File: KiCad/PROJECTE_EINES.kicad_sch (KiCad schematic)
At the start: 5 parts, among them J3 J_DEBUG

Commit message: Correció etapa d'alimentació e Inputs
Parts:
- renumbered J3 to J1, J_MOTOR_DOOR to J_MOTOR_DOOR1, R2 to R1
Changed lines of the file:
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@@
 		(dnp no)
 		(fields_autoplaced yes)
-		(property "Reference" "#PWR05"
+		(property "Reference" "#PWR01"
 			(at 26.67 107.95 0)
 			(effects
@@
 			(project ""
 				(path "/347831db-5db9-4aff-ad32-e56fd770e219"
-					(reference "#PWR05")
+					(reference "#PWR01")
 					(unit 1)
 				)
@@
 		(dnp no)
 		(fields_autoplaced yes)
-		(property "Reference" "#PWR06"
+		(property "Reference" "#PWR05"
 			(at 49.53 109.22 0)
 			(effects
@@
 			(project ""
 				(path "/347831db-5db9-4aff-ad32-e56fd770e219"
-					(reference "#PWR06")
+					(reference "#PWR05")
 					(unit 1)
 				)
@@
 		(dnp no)
 		(fields_autoplaced yes)
-		(property "Reference" "#PWR012"
+		(property "Reference" "#PWR02"
 			(at 30.48 54.61 0)
 			(effects
@@
 			(project "PROJECTE_EINES"
 				(path "/347831db-5db9-4aff-ad32-e56fd770e219"
-					(reference "#PWR012")
+					(reference "#PWR02")
 					(unit 1)
 				)
@@
 		(on_board yes)
 		(dnp no)
-		(property "Reference" "J3"
+		(property "Reference" "J1"
 			(at 22.225 16.51 0)
 			(effects
@@
 			(project "PROJECTE_EINES"
 				(path "/347831db-5db9-4aff-ad32-e56fd770e219"
-					(reference "J3")
+					(reference "J1")
 					(unit 1)
 				)
@@
 		(dnp no)
 		(fields_autoplaced yes)
-		(property "Reference" "#PWR014"
+		(property "Reference" "#PWR03"
 			(at 40.64 27.94 0)
 			(effects
@@
 			(project ""
 				(path "/347831db-5db9-4aff-ad32-e56fd770e219"
-					(reference "#PWR014")
+					(reference "#PWR03")
 					(unit 1)
 				)
@@
 		(dnp no)
 		(fields_autoplaced yes)
-		(property "Reference" "J_MOTOR_DOOR"
+		(property "Reference" "J_MOTOR_DOOR1"
 			(at 22.225 72.39 0)
 			(effects
@@
 			(project "PROJECTE_EINES"
 				(path "/347831db-5db9-4aff-ad32-e56fd770e219"
-					(reference "J_MOTOR_DOOR")
+					(reference "J_MOTOR_DOOR1")
 					(unit 1)
 				)
@@
 		(dnp no)
 		(fields_autoplaced yes)
-		(property "Reference" "R2"
+		(property "Reference" "R1"
 			(at 38.1 95.25 90)
 			(effects
@@
 			(project "PROJECTE_EINES"
 				(path "/347831db-5db9-4aff-ad32-e56fd770e219"
-					(reference "R2")
+					(reference "R1")
 					(unit 1)
 				)
@@
 		(dnp no)
 		(fields_autoplaced yes)
-		(property "Reference" "#PWR07"
+		(property "Reference" "#PWR04"
 			(at 40.64 34.29 0)
 			(effects
@@
 			(project "PROJECTE_EINES"
 				(path "/347831db-5db9-4aff-ad32-e56fd770e219"
-					(reference "#PWR07")
-					(unit 1)
-				)
+					(reference "#PWR04")
+					(unit 1)
+				)

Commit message: Actualizació Footprints
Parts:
- J_DEBUG1: renamed from J1; value J_DEBUG -> Conn_01x05_Pin; footprint (none) -> Connector_PinHeader_2.54mm:PinHeader_1x05_P2.54mm_Vertical
- J_MOTOR_DOOR1, J_MOTOR_WIN1, J_PWR1: footprint (none) -> TerminalBlock:TerminalBlock_MaiXu_MX126-5.0-02P_1x02_P5.00mm
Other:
- sheet ETAPA DE POTÈNCIA renamed ETAPA DE ALIMENTACIÓ
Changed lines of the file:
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@@
 			)
 		)
-		(property "Footprint" ""
+		(property "Footprint" "TerminalBlock:TerminalBlock_MaiXu_MX126-5.0-02P_1x02_P5.00mm"
 			(at 21.59 63.5 0)
 			(effects
@@
 		(on_board yes)
 		(dnp no)
-		(property "Reference" "J1"
+		(property "Reference" "J_DEBUG1"
 			(at 22.225 16.51 0)
 			(effects
@@
 			)
 		)
-		(property "Value" "J_DEBUG"
+		(property "Value" "Conn_01x05_Pin"
 			(at 22.225 19.05 0)
 			(effects
@@
 			)
 		)
-		(property "Footprint" ""
+		(property "Footprint" "Connector_PinHeader_2.54mm:PinHeader_1x05_P2.54mm_Vertical"
 			(at 21.59 26.67 0)
 			(effects
@@
 			(project "PROJECTE_EINES"
 				(path "/347831db-5db9-4aff-ad32-e56fd770e219"
-					(reference "J1")
+					(reference "J_DEBUG1")
 					(unit 1)
 				)
@@
 			)
 		)
-		(property "Footprint" ""
+		(property "Footprint" "TerminalBlock:TerminalBlock_MaiXu_MX126-5.0-02P_1x02_P5.00mm"
 			(at 22.86 44.45 0)
 			(effects
@@
 			)
 		)
-		(property "Footprint" ""
+		(property "Footprint" "TerminalBlock:TerminalBlock_MaiXu_MX126-5.0-02P_1x02_P5.00mm"
 			(at 21.59 77.47 0)
 			(effects
@@
 			(color 0 0 0 0.0000)
 		)
-		(property "Sheetname" "ETAPA DE POTÈNCIA"
+		(property "Sheetname" "ETAPA DE ALIMENTACIÓ"
 			(at 72.39 19.6084 0)
 			(effects

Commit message: Versió final Esquematic
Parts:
- R1: footprint (none) -> Resistor_SMD:R_0805_2012Metric
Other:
- sheet BUS CAN renamed COMUNICACIONS
- sheet SENSOR DE CORRENT renamed SENSORS
- removed sheet DRIVER DEL MOTOR FINESTRA
- removed sheet DRIVER MOTOR PORTA
- removed sheet ETAPA DE ALIMENTACIÓ
- removed sheet SENSOR RFID
- added sheet ETAPA DE ALIMENTACIO (ETAPA_ALIMENTACIO_sch.kicad_sch)
- added sheet ETAPA DE POTENCIA (ETAPA_POTENICA.kicad_sch)
- sheet COMUNICACIONS ports: added CAN_RX, CAN_TX; removed CANRX, CANTX
- sheet INPUTS ports: added DOOR_BTN_CLOSED, DOOR_BTN_OPEN, DOOR_LOCK_SW, DOOR_UNLOCK_SW; removed none
- sheet MICROCONTROLADOR I DEBUG ports: added CAN_RX, CAN_TX, DOOR_BTN_CLOSED, DOOR_BTN_OPEN, DOOR_DIAGA, DOOR_DIAGB, DOOR_INA, DOOR_INB, DOOR_LIMIT_CLOSE, DOOR_LIMIT_OPEN, DOOR_LOCK_SW, DOOR_PWM, DOOR_UNLOCK_SW; removed GND
- sheet SENSORS ports: added RFID_CS, RFID_MISO, RFID_MOSI, RFID_RST, RFID_SCK, WIN_CURRENT_ADC; removed NO
- note added: "POTENCIA"
- note added: "SENSORS"
- note removed: "MOTOR FINESTRA"
- note removed: "MOTOR PORTA"
- note removed: "SENSOR FINAL DE CARRERA"
- note removed: "SENSOR RFID"
- moved on the sheet: R1

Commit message: 1ra versióPCB
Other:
- sheet ETAPA DE POTENCIA ports: added DOOR_MOTOR_A, DOOR_MOTOR_B, WIN_MOTOR_A, WIN_MOTOR_B; removed DOOR_OUTA, DOOR_OUTB, WIN_OUTA, WIN_OUTB
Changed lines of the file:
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@@
 		)
 	)
-	(global_label "WIN_OUTA"
+	(global_label "WIN_MOTOR_B"
 		(shape output)
 		(at 248.92 107.95 0)
@@
 		)
 	)
-	(global_label "DOOR_OUTA"
+	(global_label "DOOR_MOTOR_A"
 		(shape output)
 		(at 201.93 104.14 180)
@@
 		)
 	)
-	(global_label "WIN_OUTB"
+	(global_label "WIN_MOTOR_A"
 		(shape output)
 		(at 248.92 104.14 0)
@@
 		)
 	)
-	(global_label "DOOR_OUTB"
+	(global_label "DOOR_MOTOR_B"
 		(shape output)
 		(at 201.93 107.95 180)
@@
 			)
 		)
-		(pin "DOOR_OUTA" output
+		(pin "DOOR_MOTOR_A" output
 			(at 201.93 104.14 180)
 			(effects
@@
 			)
 		)
-		(pin "DOOR_OUTB" output
+		(pin "DOOR_MOTOR_B" output
 			(at 201.93 107.95 180)
 			(effects
@@
 			)
 		)
-		(pin "WIN_OUTA" output
+		(pin "WIN_MOTOR_A" output
 			(at 248.92 107.95 0)
 			(effects
@@
 			)
 		)
-		(pin "WIN_OUTB" output
+		(pin "WIN_MOTOR_B" output
 			(at 248.92 104.14 0)
 			(effects

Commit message: Inputs
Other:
- sheet INPUTS ports: added DOOR_LOCK/UNLOCK; removed DOOR_BTN_CLOSED, DOOR_BTN_OPEN, DOOR_LOCK_SW, DOOR_UNLOCK_SW
- sheet MICROCONTROLADOR I DEBUG ports: added DOOR_LOCK/UNLOCK; removed DOOR_BTN_CLOSED, DOOR_BTN_OPEN, DOOR_LOCK_SW, DOOR_UNLOCK_SW
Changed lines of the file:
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@@
-		)
-	)
-	(global_label "DOOR_LOCK_SW"
-		(shape input)
-		(at 153.67 125.73 0)
-		(effects
-			(font
-				(size 1.27 1.27)
-			)
-			(justify left)
-		)
-		(property "Intersheetrefs" "${INTERSHEET_REFS}"
-			(at 153.67 125.73 0)
-			(effects
-				(font
-					(size 1.27 1.27)
-				)
-				(hide yes)
-			)
-		)
-	)
-	(global_label "DOOR_LOCK_SW"
-		(shape output)
-		(at 248.92 147.32 0)
-		(effects
-			(font
-				(size 1.27 1.27)
-			)
-			(justify left)
-		)
-		(property "Intersheetrefs" "${INTERSHEET_REFS}"
-			(at 248.92 147.32 0)
-			(effects
-				(font
-					(size 1.27 1.27)
-				)
-				(hide yes)
-			)
 		)
 	)
@@
 		(property "Intersheetrefs" "${INTERSHEET_REFS}"
 			(at 248.92 76.2 0)
-			(effects
-				(font
-					(size 1.27 1.27)
-				)
-				(hide yes)
-			)
-		)
-	)
-	(global_label "DOOR_BTN_OPEN"
-		(shape input)
-		(at 153.67 123.19 0)
-		(effects
-			(font
-				(size 1.27 1.27)
-			)
-			(justify left)
-		)
-		(property "Intersheetrefs" "${INTERSHEET_REFS}"
-			(at 153.67 123.19 0)
 			(effects
 				(font
@@
 		)
 	)
-	(global_label "DOOR_UNLOCK_SW"
-		(shape output)
-		(at 248.92 149.86 0)
-		(effects
-			(font
-				(size 1.27 1.27)
-			)
-			(justify left)
-		)
-		(property "Intersheetrefs" "${INTERSHEET_REFS}"
-			(at 248.92 149.86 0)
-			(effects
-				(font
-					(size 1.27 1.27)
-				)
-				(hide yes)
-			)
-		)
-	)
 	(global_label "UART_TX"
 		(shape output)
@@
 		(property "Intersheetrefs" "${INTERSHEET_REFS}"
 			(at 82.55 113.03 0)
-			(effects
-				(font
-					(size 1.27 1.27)
-				)
-				(hide yes)
-			)
-		)
-	)
-	(global_label "DOOR_UNLOCK_SW"
-		(shape input)
-		(at 153.67 128.27 0)
-		(effects
-			(font
-				(size 1.27 1.27)
-			)
-			(justify left)
-		)
-		(property "Intersheetrefs" "${INTERSHEET_REFS}"
-			(at 153.67 128.27 0)
 			(effects
 				(font
@@
 		)
 	)
-	(global_label "DOOR_BTN_CLOSED"
-		(shape input)
-		(at 153.67 120.65 0)
-		(effects
-			(font
-				(size 1.27 1.27)
-			)
-			(justify left)
-		)
-		(property "Intersheetrefs" "${INTERSHEET_REFS}"
-			(at 153.67 120.65 0)
-			(effects
-				(font
-					(size 1.27 1.27)
-				)
-				(hide yes)
-			)
-		)
-	)
 	(global_label "WIN_MOTOR_A"
 		(shape output)
@@
 		)
 	)
-	(global_label "DOOR_BTN_CLOSED"
-		(shape output)
-		(at 248.92 144.78 0)
-		(effects
-			(font
-				(size 1.27 1.27)
-			)
-			(justify left)
-		)
-		(property "Intersheetrefs" "${INTERSHEET_REFS}"
-			(at 248.92 144.78 0)
-			(effects
-				(font
-					(size 1.27 1.27)
-				)
-				(hide yes)
-			)
-		)
-	)
 	(global_label "DOOR_MOTOR_B"
 		(shape output)
@@
 		)
 	)
-	(global_label "DOOR_BTN_OPEN"
-		(shape output)
-		(at 248.92 142.24 0)
-		(effects
-			(font
-				(size 1.27 1.27)
-			)
-			(justify left)
-		)
-		(property "Intersheetrefs" "${INTERSHEET_REFS}"
-			(at 248.92 142.24 0)
-			(effects
-				(font
-					(size 1.27 1.27)
-				)
-				(hide yes)
-			)
-		)
-	)
 	(global_label "RFID_MISO"
 		(shape input)
@@
 		)
 	)
+	(global_label "DOOR_LOCK{slash}UNLOCK"
+		(shape input)
+		(at 153.67 120.65 0)
+		(fields_autoplaced yes)
+		(effects
+			(font
+				(size 1.27 1.27)
+			)
+			(justify left)
+		)
+		(property "Intersheetrefs" "${INTERSHEET_REFS}"
+			(at 176.6125 120.65 0)
+			(effects
+				(font
+					(size 1.27 1.27)
+				)
+				(justify left)
+				(hide yes)
+			)
+		)
+	)
 	(global_label "WIN_BTN_UP"
 		(shape output)
@@
 					(size 1.27 1.27)
 				)
+				(hide yes)
+			)
+		)
+	)
+	(global_label "DOOR_LOCK{slash}UNLOCK"
+		(shape output)
+		(at 248.92 146.05 0)
+		(fields_autoplaced yes)
+		(effects
+			(font
+				(size 1.27 1.27)
+			)
+			(justify left)
+		)
+		(property "Intersheetrefs" "${INTERSHEET_REFS}"
+			(at 271.8625 146.05 0)
+			(effects
+				(font
+					(size 1.27 1.27)
+				)
+				(justify left)
 				(hide yes)
 			)
@@
 			)
 		)
-		(pin "DOOR_BTN_CLOSED" input
-			(at 153.67 120.65 0)
-			(effects
-				(font
-					(size 1.27 1.27)
-				)
-				(justify right)
-			)
-		)
-		(pin "DOOR_BTN_OPEN" input
-			(at 153.67 123.19 0)
-			(effects
-				(font
-					(size 1.27 1.27)
-				)
-				(justify right)
-			)
-		)
 		(pin "DOOR_DIAGA" input
 			(at 153.67 138.43 0)
@@
 			)
 		)
-		(pin "DOOR_LOCK_SW" input
-			(at 153.67 125.73 0)
-			(effects
-				(font
-					(size 1.27 1.27)
-				)
-				(justify right)
-			)
-		)
 		(pin "DOOR_PWM" output
 			(at 153.67 140.97 0)
@@
 			)
 		)
-		(pin "DOOR_UNLOCK_SW" input
-			(at 153.67 128.27 0)
+		(pin "DOOR_LOCK{slash}UNLOCK" input
+			(at 153.67 120.65 0)
 			(effects
 				(font
@@
 			)
 		)
-		(pin "DOOR_BTN_CLOSED" output
-			(at 248.92 144.78 0)
-			(effects
-				(font
-					(size 1.27 1.27)
-				)
-				(justify right)
-			)
-		)
-		(pin "DOOR_BTN_OPEN" output
-			(at 248.92 142.24 0)
-			(effects
-				(font
-					(size 1.27 1.27)
-				)
-				(justify right)
-			)
-		)
-		(pin "DOOR_LOCK_SW" output
-			(at 248.92 147.32 0)
-			(effects
-				(font
-					(size 1.27 1.27)
-				)
-				(justify right)
-			)
-		)
-		(pin "DOOR_UNLOCK_SW" output
-			(at 248.92 149.86 0)
-			(effects
-				(font
+		(pin "DOOR_LOCK{slash}UNLOCK" output
+			(at 248.92 146.05 0)
+			(effects
+				(font

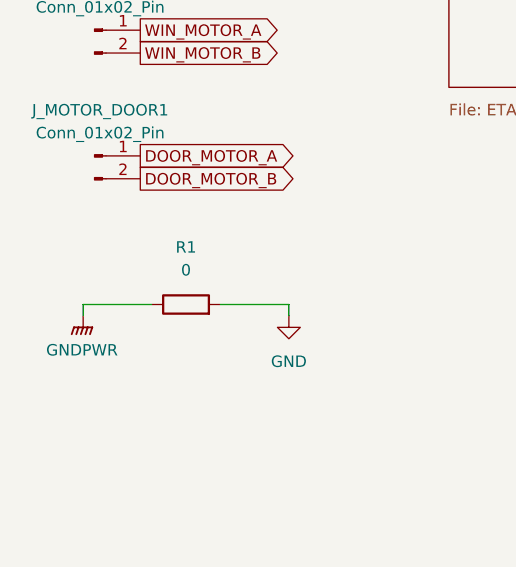
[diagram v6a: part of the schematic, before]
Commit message: Bus CAN i USART
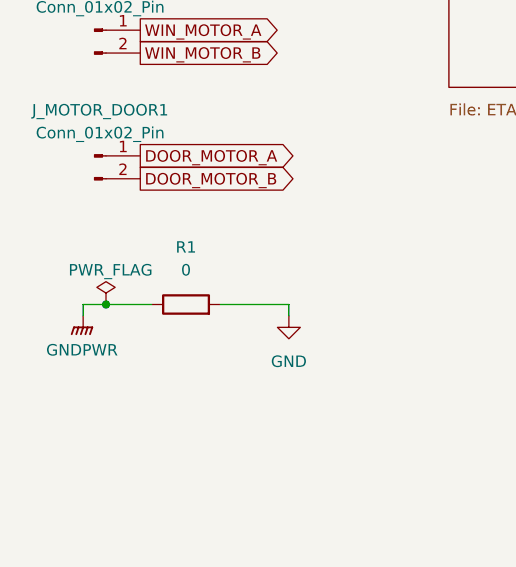
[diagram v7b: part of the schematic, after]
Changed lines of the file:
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@@
 		)
+	)
+	(junction
+		(at 22.86 93.98)
+		(diameter 0)
+		(color 0 0 0 0)
 	)
 	(wire
@@
 	(wire
 		(pts
-			(xy 20.32 93.98) (xy 27.94 93.98)
+			(xy 20.32 93.98) (xy 22.86 93.98)
 		)
 		(stroke
@@
 		(pts
 			(xy 172.72 58.42) (xy 171.45 58.42)
+		)
+		(stroke
+			(width 0)
+			(type default)
+		)
+	)
+	(wire
+		(pts
+			(xy 22.86 93.98) (xy 27.94 93.98)
 		)
 		(stroke
@@
 					(unit 1)
 				)
+			)
+		)
+	)
+	(symbol
+		(lib_id "power:PWR_FLAG")
+		(at 22.86 93.98 0)
+		(unit 1)
+		(exclude_from_sim no)
+		(in_bom yes)
+		(on_board yes)
+		(dnp no)
+		(property "Reference" "#FLG04"
+			(at 22.86 92.075 0)
+			(effects
+				(font
+					(size 1.27 1.27)
+				)
+				(hide yes)
+			)
+		)
+		(property "Value" "PWR_FLAG"
+			(at 23.368 90.17 0)
+			(effects
+				(font
+					(size 1.27 1.27)
+				)
+			)
+		)
+		(property "Footprint" ""
+			(at 22.86 93.98 0)
+			(effects
+				(font
+					(size 1.27 1.27)
+				)
+				(hide yes)
+			)
+		)
+		(property "Datasheet" "~"
+			(at 22.86 93.98 0)
+			(effects
+				(font
+					(size 1.27 1.27)
+				)
+				(hide yes)
+			)
+		)
+		(property "Description" "Special symbol for telling ERC where power comes from"
+			(at 22.86 93.98 0)
+			(effects
+				(font
+					(size 1.27 1.27)
+				)
+				(hide yes)
+			)
+		)
+		(pin "1"
+		)
+		(instances
+			(project "PROJECTE_EINES"
+				(path "/347831db-5db9-4aff-ad32-e56fd770e219"
+					(reference "#FLG04")
+					(unit 1)
+				)
